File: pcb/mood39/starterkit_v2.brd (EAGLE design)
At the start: 32 x 32 mm, 19 parts, among them IC1 TINY85, IC2 LP2950

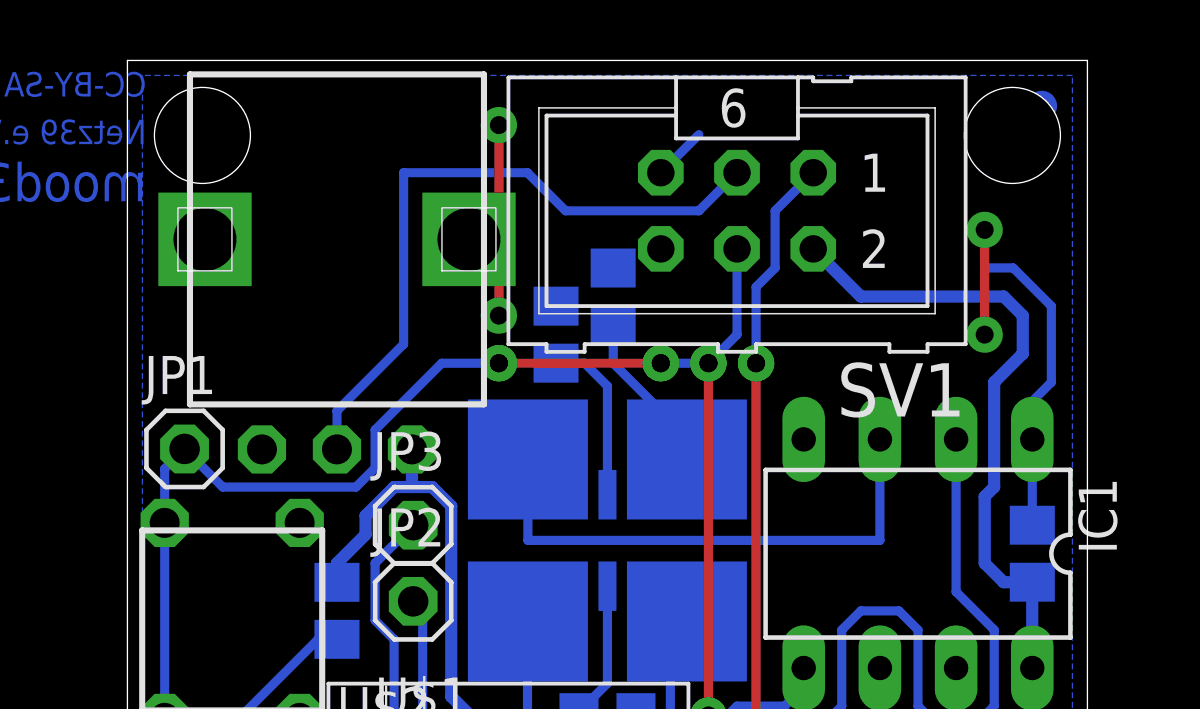
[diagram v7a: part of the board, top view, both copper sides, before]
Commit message: reduced to one problem, looks like a dead end
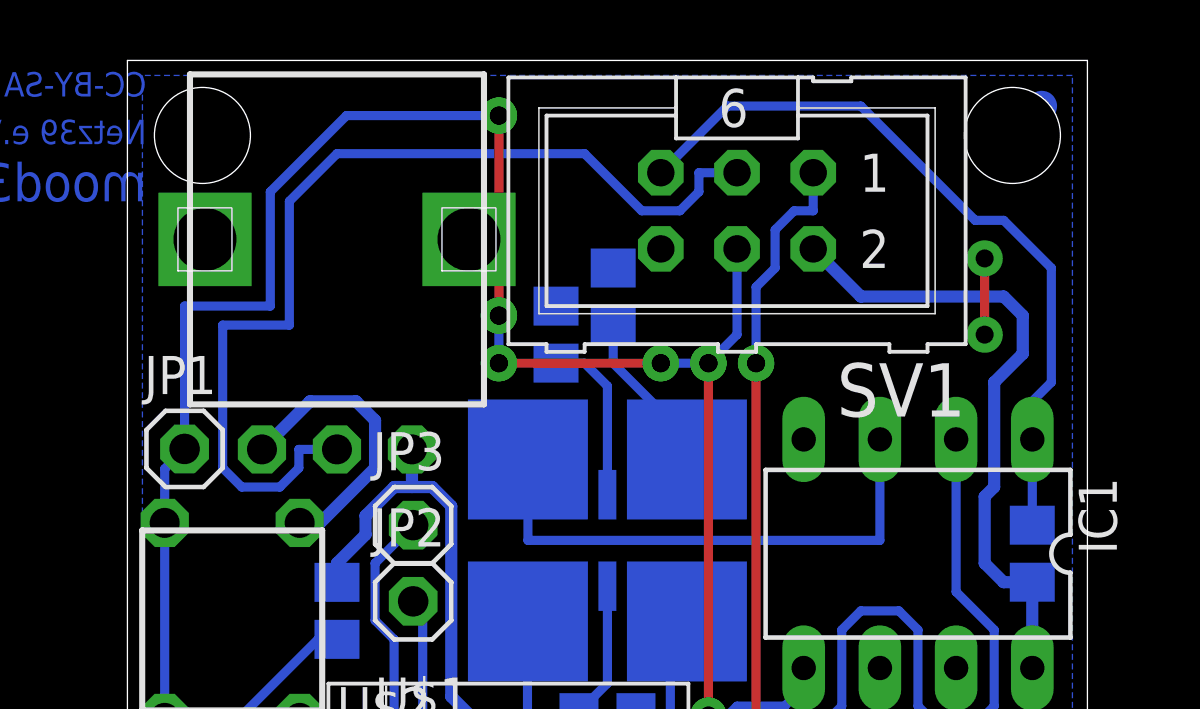
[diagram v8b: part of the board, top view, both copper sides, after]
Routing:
- net MOSI: track 49.8 -> 64.7 mm, vias 4 -> 6
- net !RESET: track 12.1 -> 25.0 mm
- net SCK: track 22.3 -> 33.3 mm
- net GND: track 22.6 -> 24.9 mm, vias 7 -> 5
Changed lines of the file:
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@@
 <contactref element="SV1" pad="1"/>
 <wire x1="13.35" y1="13.3" x2="13.35" y2="12.3675" width="0.3048" layer="16"/>
-<wire x1="22.86" y1="28.2575" x2="21.59" y2="26.9875" width="0.3048" layer="16"/>
 <via x="20.955" y="21.9075" extent="1-16" drill="0.6" shape="octagon"/>
 <wire x1="20.955" y1="21.9075" x2="20.955" y2="7.62" width="0.3048" layer="1"/>
 <via x="20.955" y="7.62" extent="1-16" drill="0.6" shape="octagon"/>
 <wire x1="13.335" y1="12.3525" x2="13.35" y2="12.3675" width="0.3048" layer="16"/>
-<wire x1="21.59" y1="26.9875" x2="21.59" y2="25.0825" width="0.3048" layer="16"/>
 <wire x1="21.59" y1="25.0825" x2="20.955" y2="24.4475" width="0.3048" layer="16"/>
 <wire x1="20.955" y1="24.4475" x2="20.955" y2="21.9075" width="0.3048" layer="16"/>
@@
 <wire x1="22.225" y1="6.35" x2="23.495" y2="6.35" width="0.3048" layer="16"/>
 <wire x1="23.495" y1="6.35" x2="25.0825" y2="7.9375" width="0.3048" layer="16"/>
+<wire x1="21.59" y1="25.0825" x2="21.59" y2="26.3525" width="0.3048" layer="16"/>
+<wire x1="21.59" y1="26.3525" x2="22.225" y2="26.9875" width="0.3048" layer="16"/>
+<wire x1="22.225" y1="26.9875" x2="22.86" y2="26.9875" width="0.3048" layer="16"/>
+<wire x1="22.86" y1="26.9875" x2="22.86" y2="28.2575" width="0.3048" layer="16"/>
 </signal>
 <signal name="PB3" class="2">
@@
 <via x="23.1775" y="7.62" extent="1-16" drill="0.6" shape="octagon"/>
 <wire x1="23.1775" y1="7.62" x2="26.67" y2="4.1275" width="0.3048" layer="1"/>
-<via x="12.3825" y="29.845" extent="1-16" drill="0.6" shape="octagon"/>
-<via x="12.3825" y="23.495" extent="1-16" drill="0.6" shape="octagon"/>
-<wire x1="12.3825" y1="29.845" x2="12.3825" y2="23.495" width="0.3048" layer="1"/>
-<via x="28.575" y="22.86" extent="1-16" drill="0.6" shape="octagon"/>
-<via x="28.575" y="26.3525" extent="1-16" drill="0.6" shape="octagon"/>
 <via x="26.67" y="4.1275" extent="1-16" drill="0.6" shape="octagon"/>
 <via x="23.1775" y="7.62" extent="1-16" drill="0.6" shape="octagon"/>
-<wire x1="28.575" y1="22.86" x2="28.575" y2="26.3525" width="0.3048" layer="1"/>
 <wire x1="23.1775" y1="7.62" x2="21.9075" y2="8.89" width="0.3048" layer="16"/>
 <wire x1="21.9075" y1="8.89" x2="20.6375" y2="8.89" width="0.3048" layer="16"/>
@@
 <wire x1="20.0025" y1="8.255" x2="18.73" y2="8.255" width="0.3048" layer="16"/>
 <wire x1="18.73" y1="8.255" x2="16.952" y2="10.16" width="0.3048" layer="16"/>
-<wire x1="5.7425" y1="16.585" x2="4.485" y2="19.035" width="0" layer="19" extent="1-1"/>
+<wire x1="4.485" y1="19.035" x2="6.0875" y2="20.6375" width="0.4064" layer="16"/>
+<wire x1="6.0875" y1="20.6375" x2="7.62" y2="20.6375" width="0.4064" layer="16"/>
+<wire x1="7.62" y1="20.6375" x2="8.255" y2="20.0025" width="0.4064" layer="16"/>
+<wire x1="8.255" y1="20.0025" x2="8.255" y2="18.415" width="0.4064" layer="16"/>
+<wire x1="8.255" y1="18.415" x2="6.425" y2="16.585" width="0.4064" layer="16"/>
+<wire x1="6.425" y1="16.585" x2="5.7425" y2="16.585" width="0.4064" layer="16"/>
+<via x="28.575" y="25.4" extent="1-16" drill="0.6" shape="octagon"/>
+<via x="28.575" y="22.86" extent="1-16" drill="0.6" shape="octagon"/>
+<wire x1="28.575" y1="25.4" x2="28.575" y2="22.86" width="0.3048" layer="1"/>
 </signal>
 <signal name="VCC" class="1">
@@
 <contactref element="SV1" pad="3"/>
 <contactref element="R5" pad="2"/>
-<wire x1="20.32" y1="28.2575" x2="19.05" y2="26.9875" width="0.3048" layer="16"/>
-<wire x1="19.05" y1="26.9875" x2="14.605" y2="26.9875" width="0.3048" layer="16"/>
-<wire x1="14.605" y1="26.9875" x2="13.335" y2="28.2575" width="0.3048" layer="16"/>
-<wire x1="13.335" y1="28.2575" x2="9.2075" y2="28.2575" width="0.3048" layer="16"/>
-<wire x1="6.985" y1="19.035" x2="6.985" y2="20.32" width="0.3048" layer="16"/>
-<wire x1="6.985" y1="20.32" x2="9.2075" y2="22.5425" width="0.3048" layer="16"/>
-<wire x1="9.2075" y1="22.5425" x2="9.2075" y2="28.2575" width="0.3048" layer="16"/>
-<wire x1="19.05" y1="26.9875" x2="27.6225" y2="11.7475" width="0" layer="19" extent="16-16"/>
+<wire x1="6.985" y1="19.035" x2="5.715" y2="19.035" width="0.3048" layer="16"/>
+<wire x1="5.715" y1="19.035" x2="5.715" y2="18.415" width="0.3048" layer="16"/>
+<wire x1="5.715" y1="18.415" x2="5.08" y2="17.78" width="0.3048" layer="16"/>
+<wire x1="5.08" y1="17.78" x2="3.81" y2="17.78" width="0.3048" layer="16"/>
+<wire x1="3.81" y1="17.78" x2="3.175" y2="18.415" width="0.3048" layer="16"/>
+<wire x1="3.175" y1="18.415" x2="3.175" y2="23.1775" width="0.3048" layer="16"/>
+<wire x1="3.175" y1="23.1775" x2="5.3975" y2="23.1775" width="0.3048" layer="16"/>
+<wire x1="5.3975" y1="23.1775" x2="5.3975" y2="27.305" width="0.3048" layer="16"/>
+<wire x1="5.3975" y1="27.305" x2="6.985" y2="28.8925" width="0.3048" layer="16"/>
+<wire x1="15.24" y1="28.8925" x2="17.145" y2="26.9875" width="0.3048" layer="16"/>
+<wire x1="17.145" y1="26.9875" x2="18.415" y2="26.9875" width="0.3048" layer="16"/>
+<wire x1="18.415" y1="26.9875" x2="19.05" y2="27.6225" width="0.3048" layer="16"/>
+<wire x1="19.05" y1="27.6225" x2="19.05" y2="28.2575" width="0.3048" layer="16"/>
+<wire x1="19.05" y1="28.2575" x2="20.32" y2="28.2575" width="0.3048" layer="16"/>
+<wire x1="15.24" y1="28.8925" x2="6.985" y2="28.8925" width="0.3048" layer="16"/>
+<wire x1="18.415" y1="26.9875" x2="27.6225" y2="11.7475" width="0" layer="19" extent="16-16"/>
 </signal>
 <signal name="MOSI" class="2">
@@
 <wire x1="19.3675" y1="21.9075" x2="20.32" y2="22.86" width="0.3048" layer="16"/>
 <wire x1="20.32" y1="22.86" x2="20.32" y2="25.7175" width="0.3048" layer="16"/>
-<wire x1="1.905" y1="19.05" x2="3.175" y2="17.78" width="0.3048" layer="16"/>
-<wire x1="3.175" y1="17.78" x2="7.62" y2="17.78" width="0.3048" layer="16"/>
-<wire x1="7.62" y1="17.78" x2="8.255" y2="18.415" width="0.3048" layer="16"/>
-<wire x1="8.255" y1="18.415" x2="8.255" y2="19.685" width="0.3048" layer="16"/>
-<wire x1="8.255" y1="19.685" x2="10.4775" y2="21.9075" width="0.3048" layer="16"/>
-<wire x1="10.4775" y1="21.9075" x2="12.3825" y2="21.9075" width="0.3048" layer="16"/>
 <via x="12.3825" y="21.9075" extent="1-16" drill="0.6" shape="octagon"/>
 <wire x1="12.3825" y1="21.9075" x2="17.78" y2="21.9075" width="0.3048" layer="1"/>
@@
 <wire x1="20.32" y1="10.4775" x2="20.0025" y2="10.16" width="0.3048" layer="16"/>
 <wire x1="20.0025" y1="10.16" x2="19.3675" y2="10.16" width="0.3048" layer="16"/>
+<wire x1="1.905" y1="19.05" x2="1.905" y2="23.8125" width="0.3048" layer="16"/>
+<wire x1="1.905" y1="23.8125" x2="4.7625" y2="23.8125" width="0.3048" layer="16"/>
+<wire x1="4.7625" y1="23.8125" x2="4.7625" y2="27.6225" width="0.3048" layer="16"/>
+<wire x1="4.7625" y1="27.6225" x2="7.3025" y2="30.1625" width="0.3048" layer="16"/>
+<via x="12.3825" y="30.1625" extent="1-16" drill="0.6" shape="octagon"/>
+<wire x1="12.3825" y1="30.1625" x2="12.3825" y2="23.495" width="0.3048" layer="1"/>
+<via x="12.3825" y="23.495" extent="1-16" drill="0.6" shape="octagon"/>
+<wire x1="12.3825" y1="23.495" x2="12.3825" y2="21.9075" width="0.3048" layer="16"/>
+<wire x1="7.3025" y1="30.1625" x2="12.3825" y2="30.1625" width="0.3048" layer="16"/>
 </signal>
 <signal name="USBD-">
@@
 <contactref element="IC1" pad="1"/>
 <contactref element="SV1" pad="5"/>
-<wire x1="17.78" y1="28.2575" x2="19.05" y2="29.5275" width="0.3048" layer="16"/>
+<wire x1="17.78" y1="28.2575" x2="20.0025" y2="30.48" width="0.3048" layer="16"/>
 <wire x1="30.1625" y1="16.5075" x2="30.1625" y2="19.3675" width="0.3048" layer="16"/>
 <wire x1="30.1625" y1="19.3675" x2="30.1625" y2="20.6375" width="0.3048" layer="16"/>
 <wire x1="30.1625" y1="20.6375" x2="30.7975" y2="21.2725" width="0.3048" layer="16"/>
-<wire x1="30.7975" y1="21.2725" x2="30.7975" y2="23.8125" width="0.3048" layer="16"/>
-<wire x1="30.7975" y1="23.8125" x2="29.5275" y2="25.0825" width="0.3048" layer="16"/>
-<wire x1="29.5275" y1="25.0825" x2="28.575" y2="25.0825" width="0.3048" layer="16"/>
-<wire x1="28.575" y1="25.0825" x2="19.05" y2="29.5275" width="0" layer="19" extent="16-16"/>
+<wire x1="30.7975" y1="21.2725" x2="30.7975" y2="25.0825" width="0.3048" layer="16"/>
+<wire x1="20.0025" y1="30.48" x2="24.4475" y2="30.48" width="0.3048" layer="16"/>
+<wire x1="24.4475" y1="30.48" x2="28.2575" y2="26.67" width="0.3048" layer="16"/>
+<wire x1="28.2575" y1="26.67" x2="29.21" y2="26.67" width="0.3048" layer="16"/>
+<wire x1="29.21" y1="26.67" x2="30.7975" y2="25.0825" width="0.3048" layer="16"/>
 </signal>
 <signal name="N$8">
@@
 <via x="12.3825" y="21.9075" extent="1-16" drill="0.6" shape="octagon"/>
 </signal>
+<signal name="N$18">
+<via x="12.3825" y="23.495" extent="1-16" drill="0.6" shape="octagon"/>
+</signal>
+<signal name="N$19">
+<via x="12.3825" y="30.1625" extent="1-16" drill="0.6" shape="octagon"/>
+</signal>
 </signals>
